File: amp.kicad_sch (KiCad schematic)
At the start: 58 parts, among them Q1 BSR56, Q2 BSR56, Q3 BC338, Q4 BC338, Q5 BC338, Q6 BC338, Q7 BC548, U2 NE5532, U3 NE5532, U4 NJM4560

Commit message: Progrees on spdif
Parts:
- removed 100u2: C_Polarized, symbol Device:C_Polarized
- added C23: 100u, symbol Device:C_Polarized
- C22: renamed from 100u1; value C_Polarized -> 100u
- C24: renamed from 100u3; value C_Polarized -> 100u
- C25: renamed from 100u4; value C_Polarized -> 100u
- renumbered C17 to C26, C18 to C27, C19 to C28, C20 to C29, C21 to C30, C22 to C31, C23 to C32, C24 to C33, C25 to C34, C26 to C35, C27 to C36, C28 to C37, R7 to R10, R8 to R11, R9 to R12, R10 to R13, R11 to R14, R12 to R15, R13 to R16, R14 to R17, R15 to R18, R16 to R19, R17 to R20, R18 to R21, R19 to R22, R20 to R23, R21 to R24, R22 to R25, R23 to R26, R24 to R27, R25 to R28, R26 to R29, R27 to R30, R28 to R31, R29 to R32, R30 to R33, R1 to R4, R2 to R5, R3 to R6, R4 to R7, R5 to R8, R6 to R9
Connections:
- net -15V: now also C22.2, C23.2; no longer C22.1
- net GND: now also C22.1, C23.1; no longer C22.2
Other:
- moved on the sheet: C22

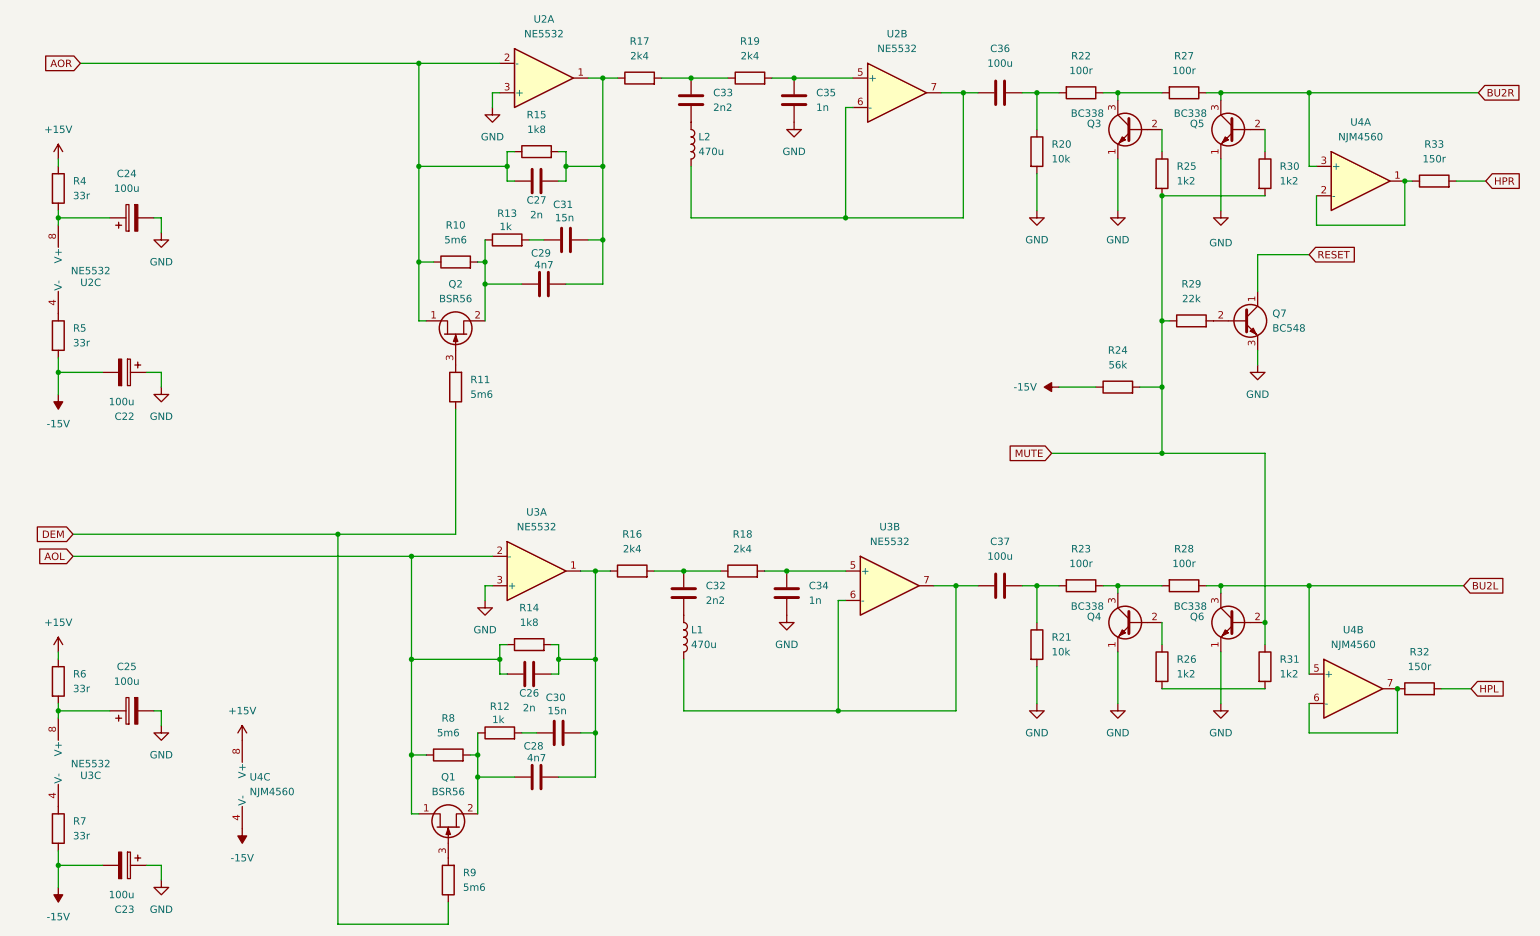
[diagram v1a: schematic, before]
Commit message: Modify DEM circuit
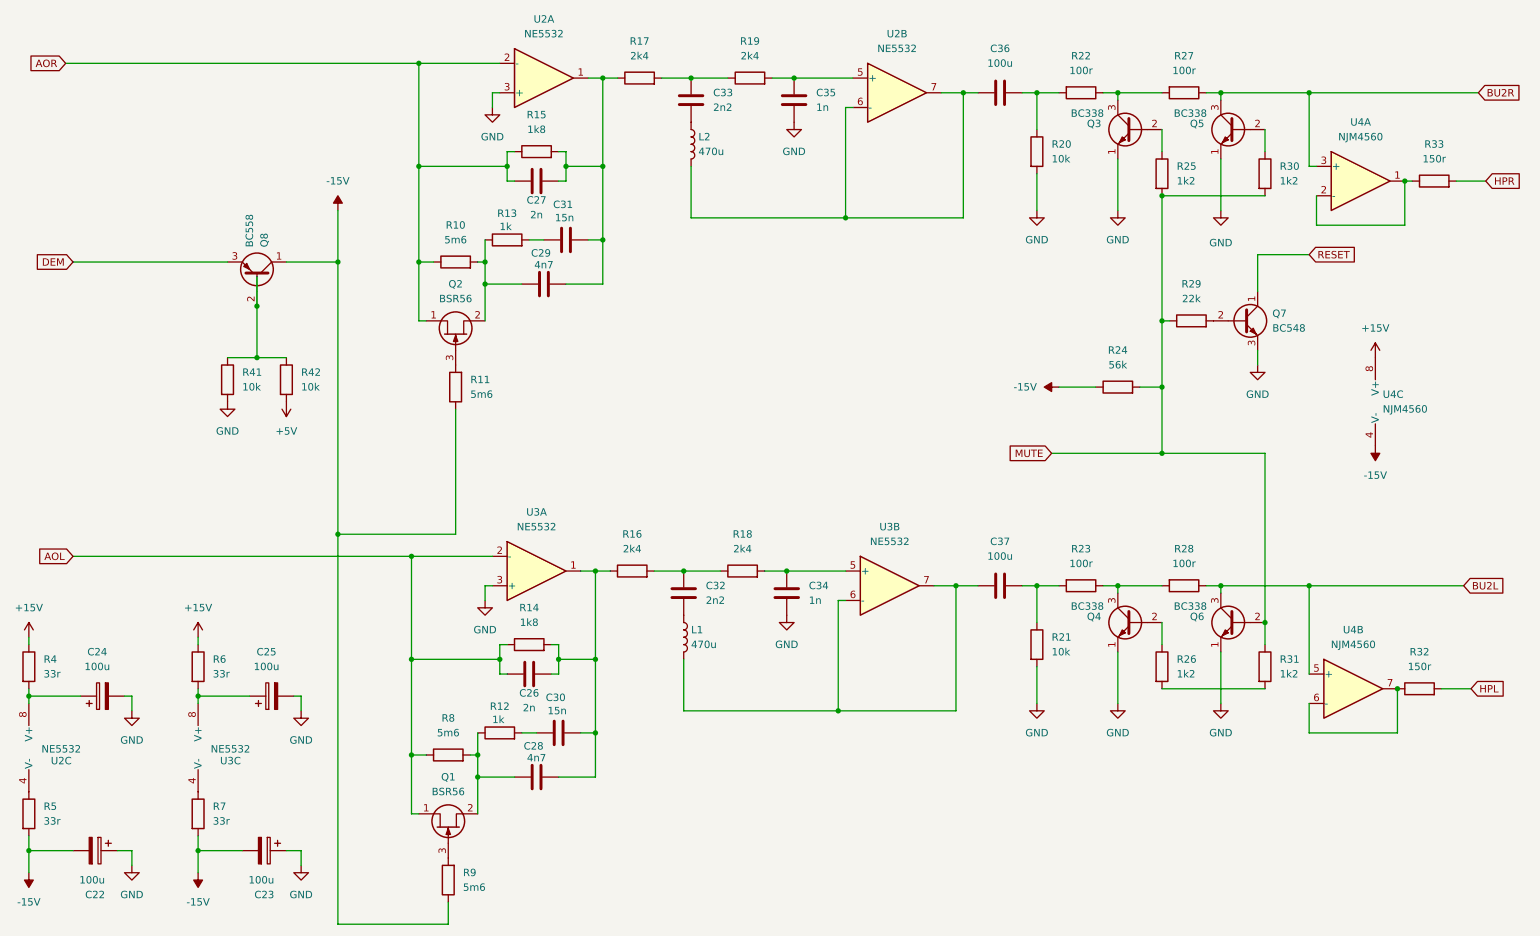
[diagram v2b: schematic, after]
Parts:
- added Q8: BC558, Package_TO_SOT_THT:TO-92, symbol Transistor_BJT:BC558
- added R41, R42: 10k, symbol Device:R
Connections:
- net -15V: now also R11.1, R9.1, Q8.1 (C)
- net DEM: now also Q8.3 (E); no longer R11.1, R9.1
- net GND: now also R41.2
- new net: Q8.2 (B), R41.1, R42.1
- new net +5V: R42.2
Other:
- moved on the sheet: C22, C23, C24, C25, R4, R5, R6, R7, U2C, U3C, U4C
